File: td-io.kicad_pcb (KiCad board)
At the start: 2 copper layers, 200 x 75 mm, 152 parts, among them J1 USB_A, J2 USB_B, J3 JAMMA_Edge, J4 Conn_Coaxial_x2, J5 DB15_Female_HighDensity_Mount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, J6 Conn_02x04_Top_Bottom, J7 Conn_02x17_Odd_Even, J8 DNP, J9 Conn_01x04_Male, Q1 AO4818B, Q2 AO4818B, Q3 AO4818B, Q4 2N7002NXBKR, Q5 2N7002NXBKR, Q6 2N7002NXBKR, SW1 SW_DPDT_x2, SW2 SW_DPDT_x2, SW3 SW_DPDT_x2, U1 TPA3138D2, U10 Pico, U11 MAX860, U12 CPC1017N, U13 74LV165, U15 LM2903, U16 PCA9306D, U2 ISL3175EIBZ-T, U3 ADA4861-3, U4 74LS86, U5 AOZ2262NQI-11, U6 74LV165, U8 74LV165, U9 74LV165

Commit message: re test zones
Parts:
- U16: footprint Package_SO:SOIC-8_3.9x4.9mm_P1.27mm -> Package_SO:SO-8_3.9x4.9mm_P1.27mm
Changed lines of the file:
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@@
     )
   )
-  (footprint "Package_SO:SOIC-8_3.9x4.9mm_P1.27mm" (layer "F.Cu")
+  (footprint "Package_SO:SO-8_3.9x4.9mm_P1.27mm" (layer "F.Cu")
     (at 201.5 104 90)
-    (descr "SOIC, 8 Pin (JEDEC MS-012AA, https://www.analog.com/media/en/package-pcb-resources/package/pkg_pdf/soic_narrow-r/r_8.pdf), generated with kicad-footprint-generator ipc_gullwing_generator.py")
-    (tags "SOIC SO")
+    (descr "SO, 8 Pin (https://www.nxp.com/docs/en/data-sheet/PCF8523.pdf), generated with kicad-footprint-generator ipc_gullwing_generator.py")
+    (tags "SO SO")
     (property "Digikey" "568-4215-1-ND")
     (property "Sheetfile" "td-io.kicad_sch")
@@
     )
     (fp_line (start 0 -2.56) (end -3.45 -2.56) (layer "F.SilkS") (width 0.12))
+    (fp_line (start 0 2.56) (end 1.95 2.56) (layer "F.SilkS") (width 0.12))
     (fp_line (start 0 2.56) (end -1.95 2.56) (layer "F.SilkS") (width 0.12))
     (fp_line (start 0 -2.56) (end 1.95 -2.56) (layer "F.SilkS") (width 0.12))
-    (fp_line (start 0 2.56) (end 1.95 2.56) (layer "F.SilkS") (width 0.12))
     (fp_line (start 3.7 -2.7) (end -3.7 -2.7) (layer "F.CrtYd") (width 0.05))
     (fp_line (start 3.7 2.7) (end 3.7 -2.7) (layer "F.CrtYd") (width 0.05))
+    (fp_line (start -3.7 -2.7) (end -3.7 2.7) (layer "F.CrtYd") (width 0.05))
     (fp_line (start -3.7 2.7) (end 3.7 2.7) (layer "F.CrtYd") (width 0.05))
-    (fp_line (start -3.7 -2.7) (end -3.7 2.7) (layer "F.CrtYd") (width 0.05))
+    (fp_line (start -1.95 2.45) (end -1.95 -1.475) (layer "F.Fab") (width 0.1))
     (fp_line (start 1.95 -2.45) (end 1.95 2.45) (layer "F.Fab") (width 0.1))
+    (fp_line (start -0.975 -2.45) (end 1.95 -2.45) (layer "F.Fab") (width 0.1))
+    (fp_line (start -1.95 -1.475) (end -0.975 -2.45) (layer "F.Fab") (width 0.1))
     (fp_line (start 1.95 2.45) (end -1.95 2.45) (layer "F.Fab") (width 0.1))
-    (fp_line (start -0.975 -2.45) (end 1.95 -2.45) (layer "F.Fab") (width 0.1))
-    (fp_line (start -1.95 2.45) (end -1.95 -1.475) (layer "F.Fab") (width 0.1))
-    (fp_line (start -1.95 -1.475) (end -0.975 -2.45) (layer "F.Fab") (width 0.1))
-    (pad "1" smd roundrect (at -2.475 -1.905 90) (size 1.95 0.6) (layers "F.Cu" "F.Paste" "F.Mask") (roundrect_rratio 0.25)
+    (pad "1" smd roundrect (at -2.575 -1.905 90) (size 1.75 0.6) (layers "F.Cu" "F.Paste" "F.Mask") (roundrect_rratio 0.25)
       (net 1 "GND") (pinfunction "GND") (pintype "power_in"))
-    (pad "2" smd roundrect (at -2.475 -0.635 90) (size 1.95 0.6) (layers "F.Cu" "F.Paste" "F.Mask") (roundrect_rratio 0.25)
+    (pad "2" smd roundrect (at -2.575 -0.635 90) (size 1.75 0.6) (layers "F.Cu" "F.Paste" "F.Mask") (roundrect_rratio 0.25)
       (net 8 "+3V3") (pinfunction "VREF1") (pintype "power_in"))
-    (pad "3" smd roundrect (at -2.475 0.635 90) (size 1.95 0.6) (layers "F.Cu" "F.Paste" "F.Mask") (roundrect_rratio 0.25)
+    (pad "3" smd roundrect (at -2.575 0.635 90) (size 1.75 0.6) (layers "F.Cu" "F.Paste" "F.Mask") (roundrect_rratio 0.25)
       (net 183 "/i2c_scl") (pinfunction "SCL1") (pintype "bidirectional"))
-    (pad "4" smd roundrect (at -2.475 1.905 90) (size 1.95 0.6) (layers "F.Cu" "F.Paste" "F.Mask") (roundrect_rratio 0.25)
+    (pad "4" smd roundrect (at -2.575 1.905 90) (size 1.75 0.6) (layers "F.Cu" "F.Paste" "F.Mask") (roundrect_rratio 0.25)
       (net 182 "/i2c_sda") (pinfunction "SDA1") (pintype "bidirectional"))
-    (pad "5" smd roundrect (at 2.475 1.905 90) (size 1.95 0.6) (layers "F.Cu" "F.Paste" "F.Mask") (roundrect_rratio 0.25)
+    (pad "5" smd roundrect (at 2.575 1.905 90) (size 1.75 0.6) (layers "F.Cu" "F.Paste" "F.Mask") (roundrect_rratio 0.25)
       (net 181 "/vga_sda") (pinfunction "SDA2") (pintype "bidirectional"))
-    (pad "6" smd roundrect (at 2.475 0.635 90) (size 1.95 0.6) (layers "F.Cu" "F.Paste" "F.Mask") (roundrect_rratio 0.25)
+    (pad "6" smd roundrect (at 2.575 0.635 90) (size 1.75 0.6) (layers "F.Cu" "F.Paste" "F.Mask") (roundrect_rratio 0.25)
       (net 180 "/vga_scl") (pinfunction "SCL2") (pintype "bidirectional"))
-    (pad "7" smd roundrect (at 2.475 -0.635 90) (size 1.95 0.6) (layers "F.Cu" "F.Paste" "F.Mask") (roundrect_rratio 0.25)
+    (pad "7" smd roundrect (at 2.575 -0.635 90) (size 1.75 0.6) (layers "F.Cu" "F.Paste" "F.Mask") (roundrect_rratio 0.25)
       (net 12 "Net-(C7-Pad1)") (pinfunction "VREF2") (pintype "power_in"))
-    (pad "8" smd roundrect (at 2.475 -1.905 90) (size 1.95 0.6) (layers "F.Cu" "F.Paste" "F.Mask") (roundrect_rratio 0.25)
+    (pad "8" smd roundrect (at 2.575 -1.905 90) (size 1.75 0.6) (layers "F.Cu" "F.Paste" "F.Mask") (roundrect_rratio 0.25)
       (net 12 "Net-(C7-Pad1)") (pinfunction "EN") (pintype "input"))
-    (model "${KICAD6_3DMODEL_DIR}/Package_SO.3dshapes/SOIC-8_3.9x4.9mm_P1.27mm.wrl"
+    (model "${KICAD6_3DMODEL_DIR}/Package_SO.3dshapes/SO-8_3.9x4.9mm_P1.27mm.wrl"
       (offset (xyz 0 0 0))
       (scale (xyz 1 1 1))

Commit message: forking it hard
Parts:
- removed C1, C19, C2, C20, C21, C22, C23, C38, C39, C4, C40, C8: 1uF, Capacitor_SMD:C_0805_2012Metric
- removed C10, C11, C13, C14, C15, C16, C3, C32, C34, C35, C5, C6, C7: 0.1uF, Capacitor_SMD:C_0805_2012Metric
- removed C12, C9: 100uF, Capacitor_SMD:C_1210_3225Metric
- removed C17, C18, C36, C37: 47uF 16V, Capacitor_SMD:C_1210_3225Metric
- removed C24, C25, C26, C27: 2.2uF 50V, Capacitor_SMD:C_1210_3225Metric
- removed C28, C30, C31, C33: 3.3uF, Capacitor_SMD:C_0805_2012Metric
- removed C29: 4.7uF, Capacitor_SMD:C_0805_2012Metric
- removed D2: BAT54C, Package_TO_SOT_SMD:SOT-23
- removed D3, D4: MMBZ18VALT1G, Package_TO_SOT_SMD:SOT-23
- removed F2, F3, F4, F5, F6: Polyfuse, Resistor_SMD:R_1812_4532Metric
- removed H1, H2, H3, H4: MountingHole_Pad, MountingHole:MountingHole_3.2mm_M3_Pad_Via
- removed J5: DB15_Female_HighDensity_MountingHoles, td-io:DSUB-15-HD_Female_Horizontal_P2.29x2.5mm_EdgePinOffset8.35mm_Housed_MountingHolesOffset10.89mm
- removed J6: Conn_02x04_Top_Bottom, td-io:B08P-VL
- removed J7: Conn_02x17_Odd_Even, td-io:DF1BZ-34DP-2.5DS
- removed J8: DNP, Connector_PinHeader_2.54mm:PinHeader_1x05_P2.54mm_Vertical
- removed J9: Conn_01x04_Male, td-io:JST_SH_B4B-NH-A_1x04_P2.50mm_Vertical
- removed L1: 1.5uH, Inductor_SMD:L_Bourns_SRP7028A_7.3x6.6mm
- removed L2, L3, L4, L5: 15uH, Inductor_SMD:L_7.3x7.3_H4.5
- removed Q2, Q3: AO4818B, Package_SO:SOIC-8_3.9x4.9mm_P1.27mm
- removed Q4, Q5, Q6: 2N7002NXBKR, Package_TO_SOT_SMD:SOT-23
- removed R1, R2, R22, R23, R24, R26, R27, R28, R29, R30, R31, R34, R35, R36, R37, R38, R39, R4, R40, R41, R42, R43, R44, R45, R46, R47, R48, R49, R51, R53, R54, R56, R57, R58, R59, R6, R61, R62, R7: 10k, Resistor_SMD:R_0805_2012Metric
- removed R10, R17, R18, R19, R8, R9: 75, Resistor_SMD:R_0805_2012Metric
- removed R11, R12, R13, R33: 330, Resistor_SMD:R_0805_2012Metric
- removed R14, R15, R16, R32: 1k, Resistor_SMD:R_0805_2012Metric
- removed R25: 20k, Resistor_SMD:R_0805_2012Metric
- removed R3, R63: 200k, Resistor_SMD:R_0805_2012Metric
- removed RV1: R_POT_Dual, td-io:PTV112-4420A-A503
- removed SW1, SW2, SW3: SW_DPDT_x2, Button_Switch_SMD:SW_DPDT_CK_JS202011JCQN
- removed U1: TPA3138D2, td-io:HTSSOP-28-1EP_4.4x9.7mm_P0.65mm_tpa3138_ThermalVias
- removed U10: Pico, td-io:RPi_Pico_SMD
- removed U11: MAX860, Package_SO:SOIC-8_3.9x4.9mm_P1.27mm
- removed U13, U6, U8, U9: 74LV165, Package_SO:SOIC-16_3.9x9.9mm_P1.27mm
- removed U15: LM2903, Package_SO:SOIC-8_3.9x4.9mm_P1.27mm
- removed U16: PCA9306D, Package_SO:SO-8_3.9x4.9mm_P1.27mm
- removed U3: ADA4861-3, Package_SO:SOIC-14_3.9x8.7mm_P1.27mm
- removed U4: 74LS86, Package_SO:SOIC-14_3.9x8.7mm_P1.27mm
- removed U5: AOZ2262NQI-11, td-io:AOS_QFN-23-2EP_4x4mm_P0.5mm
- J1: value USB_A -> Conn_01x04; footprint Connector_USB:USB_A_Molex_67643_Horizontal -> Connector_PinHeader_2.54mm:PinHeader_1x04_P2.54mm_Vertical
- J3: value JAMMA_Edge -> Conn_01x02; footprint td-io:JAMMA -> Connector_PinHeader_2.54mm:PinHeader_1x02_P2.54mm_Vertical
- J4: value Conn_Coaxial_x2 -> Conn_01x02; footprint td-io:PJRAN2X1U01AUX -> Connector_PinHeader_2.54mm:PinHeader_1x02_P2.54mm_Vertical
- moved U2 118.9 mm to (156.0, 56.0), turned to -90 degrees
- moved J3 111.2 mm to (165.0, 48.0), turned to -90 degrees
- moved J1 93.7 mm to (152.0, 48.0), turned to -90 degrees
- moved Q1 86.6 mm to (164.0, 57.0)
- moved R5 82.3 mm to (155.0, 64.0), turned to -90 degrees
- moved U12 81.0 mm to (146.0, 63.0), turned to 90 degrees
- moved R52 79.6 mm to (159.0, 64.0), turned to -90 degrees
- moved J2 78.2 mm to (181.9, 60.0)
- moved F1 75.7 mm to (171.0, 58.0), turned to 90 degrees
- moved R55 74.9 mm to (151.0, 64.0), turned to -90 degrees
- moved R50 67.7 mm to (163.0, 64.0), turned to -90 degrees
- moved D1 66.8 mm to (169.0, 64.0), turned to 90 degrees
- moved J4 33.8 mm to (145.0, 55.0), turned to 90 degrees
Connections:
- J1 pad 1: Net-(J1-Pad1) -> /jvs_rx
- J1 pad 2: Net-(J1-Pad2) -> /jvs_re
- J1 pad 3: Net-(J1-Pad3) -> /jvs_de
- J1 pad 4: GND -> /jvs_tx
- J2 pad 2: Net-(J1-Pad2) -> Net-(J2-Pad2)
- J2 pad 3: Net-(J1-Pad3) -> Net-(J2-Pad3)
- J3 pad 1: GND -> +3V3
- J4 pad 1: /r_in -> /termination
- J4 pad 2: /l_in -> /sense_0v
- Q1 pad 5: Net-(Q1-Pad5) -> unconnected-(Q1-Pad5)
- Q1 pad 6: Net-(Q1-Pad5) -> unconnected-(Q1-Pad5)
- R5 pad 1: Net-(J1-Pad3) -> Net-(J2-Pad3)
- U12 pad 4: Net-(J1-Pad2) -> Net-(J2-Pad2)
- U2 pad 6: Net-(J1-Pad3) -> Net-(J2-Pad3)
- U2 pad 7: Net-(J1-Pad2) -> Net-(J2-Pad2)
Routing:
- net +5V: track 320.1 -> 0.00 mm, vias 35 -> 0
- net +3V3: track 324.6 -> 40.2 mm, vias 10 -> 0
- net +12V: track 224.8 -> 0.00 mm, vias 7 -> 0
- net +5VL: track 154.9 -> 0.00 mm, vias 15 -> 0
- net /sr_clr: track 124.7 -> 0.00 mm, vias 8 -> 0
- net /meter2_ctl: track 124.3 -> 0.00 mm
- net /lockout2_ctl: track 119.5 -> 0.00 mm, vias 2 -> 0
- net +5VD: track 118.8 -> 0.00 mm, vias 3 -> 0
- net /meter1_ctl: track 116.0 -> 0.00 mm
- net /sr_clk: track 113.7 -> 0.00 mm, vias 8 -> 0
- net /lockout1_ctl: track 112.8 -> 0.00 mm, vias 2 -> 0
- net GND: track 108.9 -> 0.00 mm, vias 105 -> 1
- net /jamma_sync: track 103.8 -> 0.00 mm, vias 1 -> 0
- net /p1_4: track 100.2 -> 0.00 mm, vias 1 -> 0
- net /p2_4: track 99.6 -> 0.00 mm, vias 2 -> 0
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- removed copper zone on B.Cu, net +5VL
- removed copper zone on F.Cu, net +5VL
- removed copper zone on B.Cu, net /JVS Power/SW
- removed copper zone on F.Cu, net /JVS Power/SW
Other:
- board size 200 x 75 mm -> 52.2 x 23.5 mm
- board text added: "3.3v"
- board text added: "JVS"
- board text added: "JVS tranceiver buffi 2022"
- board text added: "de"
- board text added: "gnd"
- board text added: "re"
- board text added: "rx"
- board text added: "sense"
- board text added: "termination"
- board text added: "tx"
- board text removed: "+"
- board text removed: "+3.3V 8A +5V 10A +12V 2A"
- board text removed: "-"
- board text removed: "1"
- board text removed: "2"
- board text removed: "JVS ONLY"
- board text removed: "L"
- board text removed: "R"
- board text removed: "adc"
- board text removed: "coin chutes"
- board text removed: "mono"
- board text removed: "on"
- board text removed: "speaker output"
- board text removed: "stereo"
- board text removed: "td-io v1.3 2022 https://github.com/tdaede/td-io CERN-OHL-W"
- board text removed: "volume"

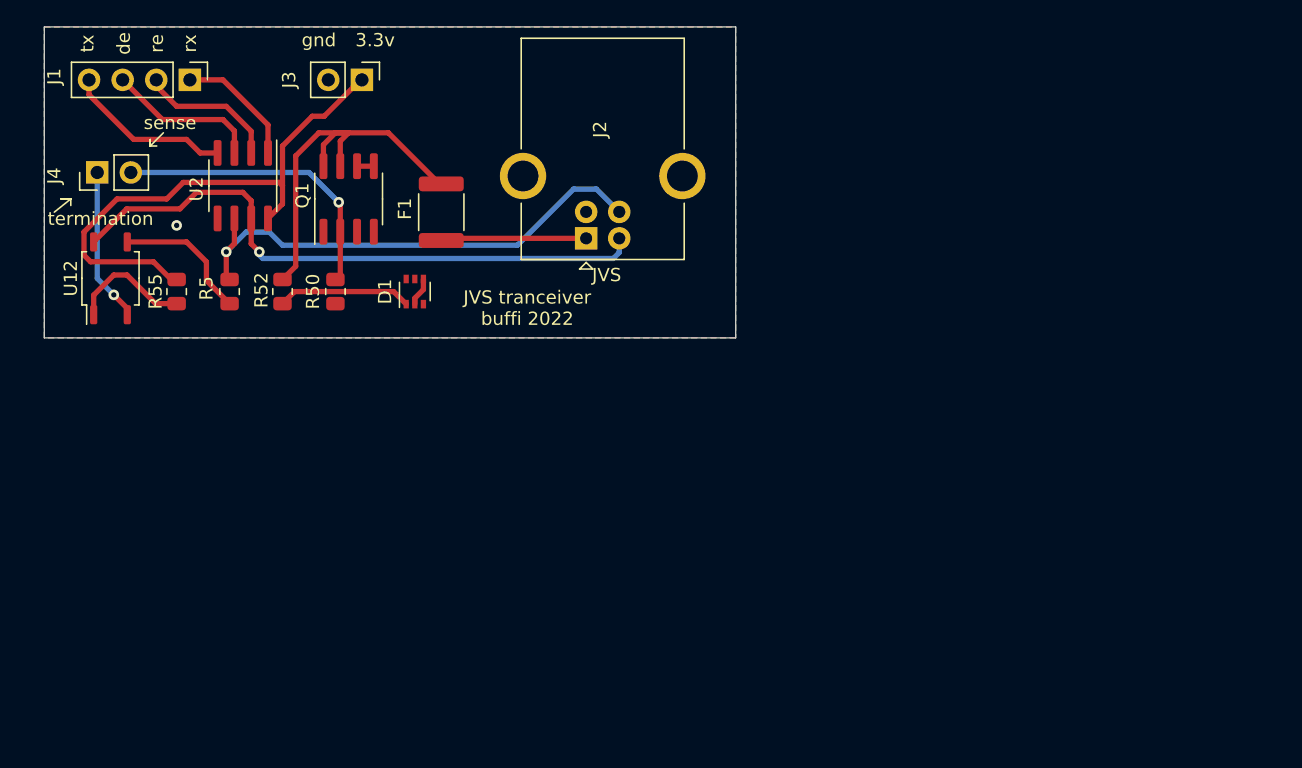
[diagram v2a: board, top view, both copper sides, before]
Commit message: Updated pcb with onboard pico
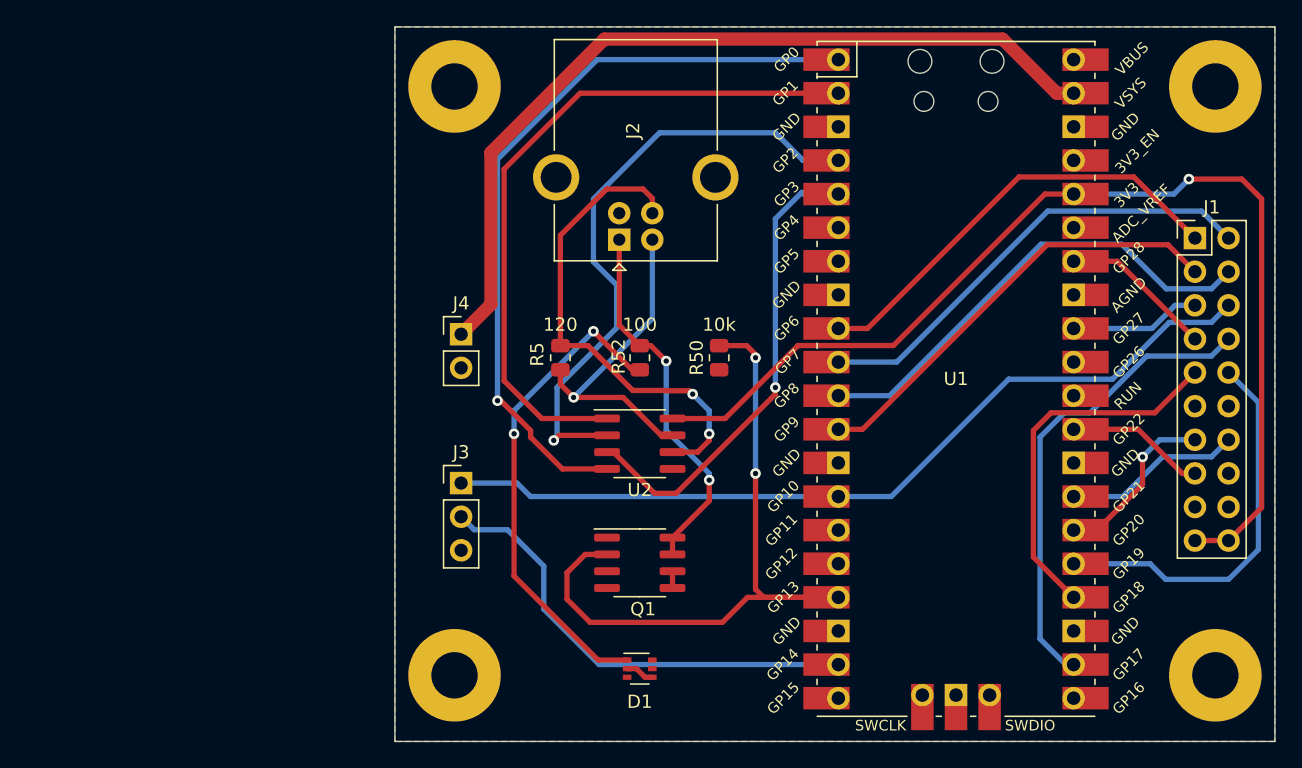
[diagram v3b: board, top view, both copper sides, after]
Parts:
- removed F1: Polyfuse, Resistor_SMD:R_1812_4532Metric
- removed R55: 1k, Resistor_SMD:R_0805_2012Metric
- removed U12: CPC1017N, Package_SO:SOP-4_3.8x4.1mm_P2.54mm
- added H1: MountingHole_Pad, MountingHole:MountingHole_3.5mm_Pad, F.Cu at (172.0, 48.5)
- added H2: MountingHole_Pad, MountingHole:MountingHole_3.5mm_Pad, F.Cu at (229.5, 48.5)
- added H3: MountingHole_Pad, MountingHole:MountingHole_3.5mm_Pad, F.Cu at (172.0, 93.0)
- added H4: MountingHole_Pad, MountingHole:MountingHole_3.5mm_Pad, F.Cu at (229.5, 93.0)
- added U1: Pico, RPi_Pico:RPi_Pico_SMD_TH, F.Cu at (209.9, 70.6)
- J1: value Conn_01x04 -> Conn_02x10_Odd_Even; footprint Connector_PinHeader_2.54mm:PinHeader_1x04_P2.54mm_Vertical -> Connector_PinHeader_2.54mm:PinHeader_2x10_P2.54mm_Vertical
- J3: value Conn_01x02 -> Conn_01x03; footprint Connector_PinHeader_2.54mm:PinHeader_1x02_P2.54mm_Vertical -> Connector_PinHeader_2.54mm:PinHeader_1x03_P2.54mm_Vertical
- moved J1 76.9 mm to (228.0, 60.0), turned to 0 degrees
- moved U2 35.8 mm to (186.0, 75.5), turned to 0 degrees
- moved Q1 35.2 mm to (186.0, 84.5), turned to 0 degrees
- moved D1 33.2 mm to (186.0, 92.5), turned to 0 degrees
- moved J3 31.4 mm to (172.5, 78.5), turned to 0 degrees
- moved J4 30.1 mm to (172.5, 67.2), turned to 0 degrees
- moved R50 29.4 mm to (192.0, 69.0)
- moved R52 27.5 mm to (186.0, 69.0)
- moved R5 25.5 mm to (180.0, 69.0)
- moved J2 2.50 mm to (184.4, 60.1)
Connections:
- J1 pad 1: /jvs_rx -> /b_up
- J1 pad 2: /jvs_re -> /b_down
- J1 pad 3: /jvs_de -> /b_right
- J1 pad 4: /jvs_tx -> /b_left
- J2 pad 1: Net-(F1-Pad1) -> Net-(J2-Pad1)
- J3 pad 1: +3V3 -> /b_test
- J3 pad 2: GND -> /b_service
- J4 pad 1: /termination -> +5V
- J4 pad 2: /sense_0v -> GND
- Q1 pad 7: Net-(F1-Pad2) -> Net-(J2-Pad1)
- Q1 pad 8: Net-(F1-Pad2) -> Net-(J2-Pad1)
- R5 pad 2: Net-(R5-Pad2) -> Net-(J2-Pad2)
- R52 pad 1: Net-(F1-Pad2) -> Net-(J2-Pad1)
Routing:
- net /b_test: track 0.00 -> 64.4 mm
- net +5V: track 0.00 -> 63.9 mm
- net /jvs_tx: track 12.7 -> 57.8 mm, vias 0 -> 1
- net /jvs_rx: track 9.44 -> 52.6 mm
- net +3V3: track 40.2 -> 82.0 mm, vias 0 -> 1
- net /b_left: track 0.00 -> 36.2 mm
- net /b_1: track 0.00 -> 35.9 mm
- net /jvs_re: track 10.7 -> 46.6 mm, vias 0 -> 1
- net /b_down: track 0.00 -> 35.1 mm
- net /b_service: track 0.00 -> 35.0 mm
- net /b_up: track 0.00 -> 33.6 mm
- net /b_right: track 0.00 -> 33.6 mm
- net /sense_0v: track 22.7 -> 54.9 mm, vias 1 -> 2
- net /b_3: track 0.00 -> 29.7 mm
- net Net-(F1-Pad2): track 29.5 -> 0.00 mm
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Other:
- board size 52.2 x 23.5 mm -> 66.5 x 54 mm
- board text removed: "3.3v"
- board text removed: "JVS"
- board text removed: "JVS tranceiver buffi 2022"
- board text removed: "de"
- board text removed: "gnd"
- board text removed: "re"
- board text removed: "rx"
- board text removed: "sense"
- board text removed: "termination"
- board text removed: "tx"
